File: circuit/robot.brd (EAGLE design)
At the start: 26 x 33 mm, 11 parts, among them M1 SERVO-FLIPPED, M2 SERVO-1, M3 SERVO-1, U1 ESP01

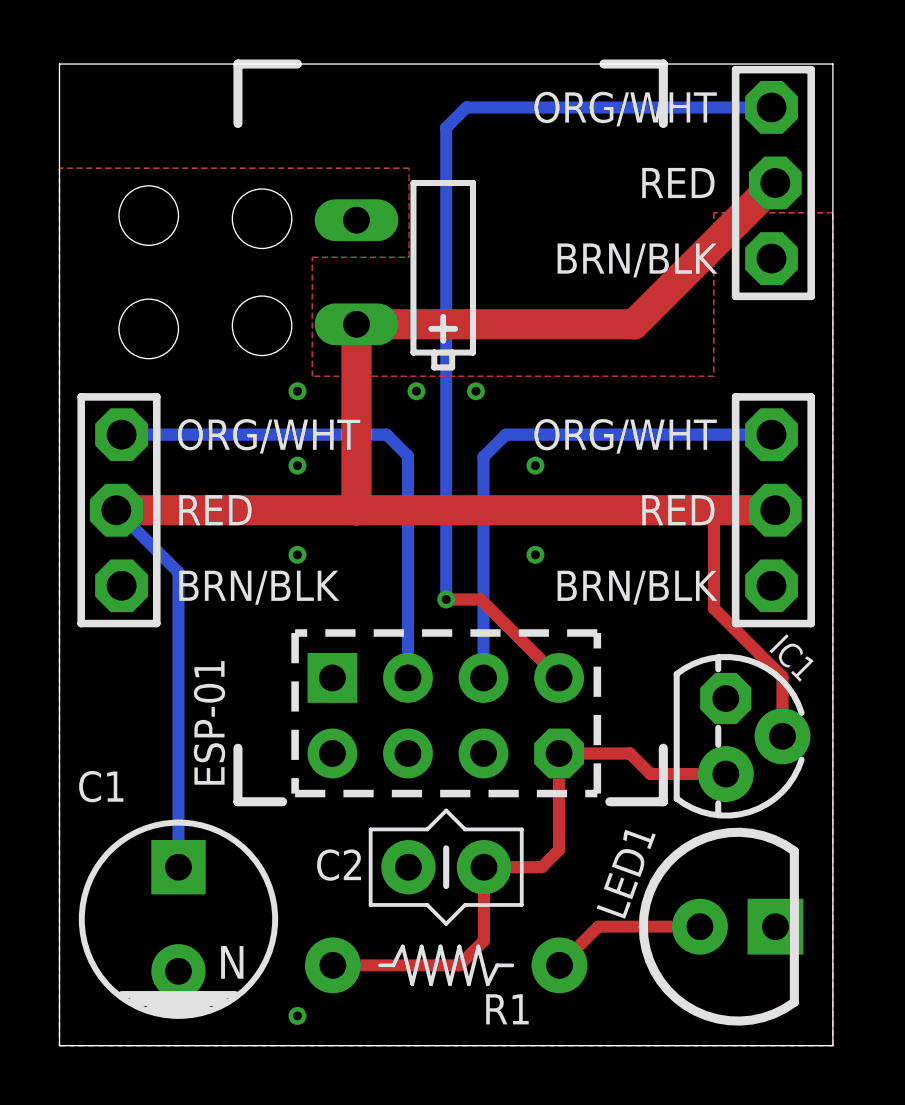
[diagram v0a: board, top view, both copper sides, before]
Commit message: update small PCB with version info
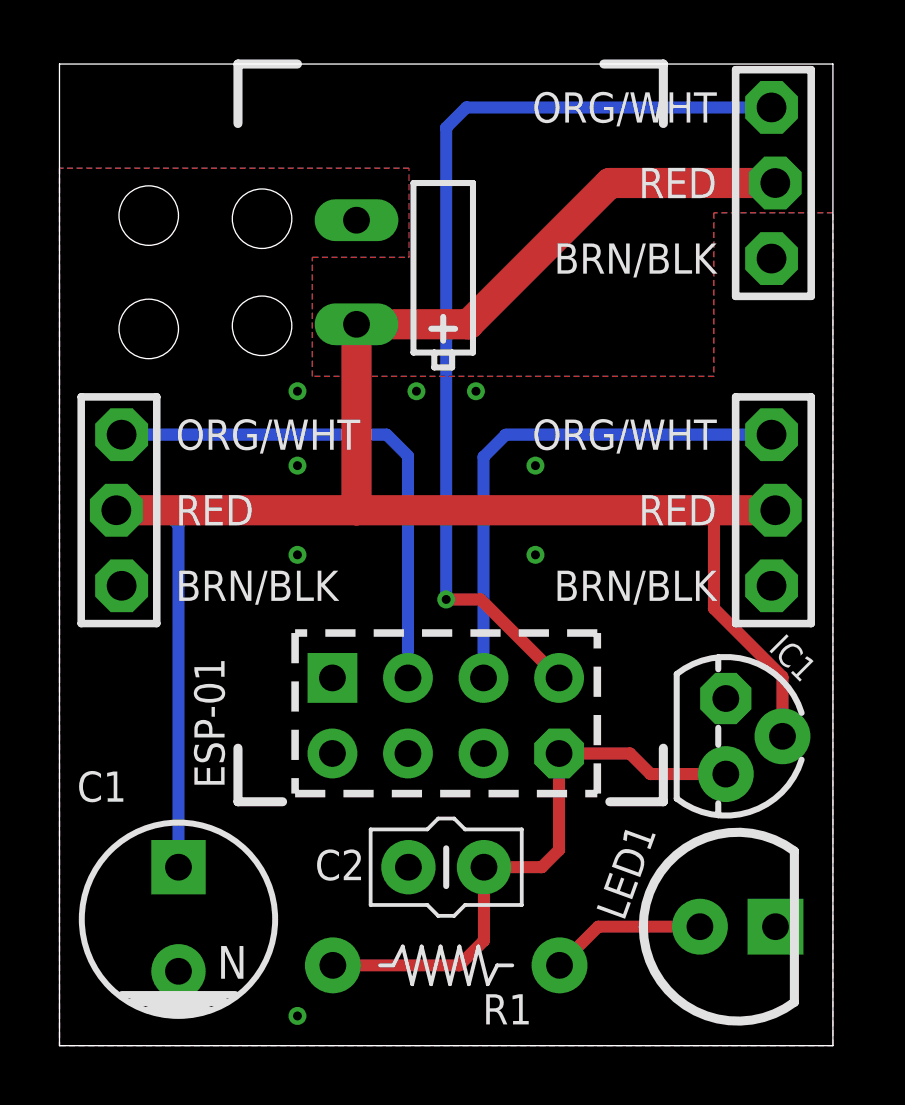
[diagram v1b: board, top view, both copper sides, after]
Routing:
- net +6V: track 65.9 -> 66.8 mm
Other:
- board text added: "SSF.NET/LIBRARY ROBOT-2019-REV1"
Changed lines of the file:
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@@
 <text x="5.3" y="2.25" size="1.1" layer="21" font="vector" ratio="12">N</text>
 <text x="5.55" y="8.65" size="1.016" layer="25" ratio="12" rot="R90">ESP-01</text>
+<text x="19.5" y="32.5" size="1.016" layer="22" rot="MR270">SSF.NET/LIBRARY
+ROBOT-2019-REV1</text>
 </plain>
 <attributes>
@@
 <wire x1="24.0635" y1="18" x2="22" y2="18" width="1.016" layer="1"/>
 <wire x1="22" y1="18" x2="9.985" y2="18" width="1.016" layer="1"/>
-<wire x1="24.0635" y1="29" x2="19.3135" y2="24.25" width="1.016" layer="1"/>
-<wire x1="19.3135" y1="24.25" x2="9.985" y2="24.25" width="1.016" layer="1"/>
 <wire x1="24.305" y1="10.4" x2="24.305" y2="12.395" width="0.4064" layer="1"/>
 <wire x1="24.305" y1="12.395" x2="22" y2="14.7" width="0.4064" layer="1"/>
 <wire x1="22" y1="14.7" x2="22" y2="18" width="0.4064" layer="1"/>
-<wire x1="4" y1="6" x2="4" y2="15.9111" width="0.4064" layer="16"/>
-<wire x1="4" y1="15.9111" x2="1.9111" y2="18" width="0.4064" layer="16"/>
+<wire x1="4" y1="6" x2="4" y2="17.5" width="0.4064" layer="16"/>
+<wire x1="4" y1="17.5" x2="3.5" y2="18" width="0.4064" layer="16"/>
+<wire x1="3.5" y1="18" x2="1.9111" y2="18" width="0.4064" layer="16"/>
+<wire x1="9.985" y1="24.25" x2="13.75" y2="24.25" width="1.016" layer="1"/>
+<wire x1="13.75" y1="24.25" x2="18.5" y2="29" width="1.016" layer="1"/>
+<wire x1="18.5" y1="29" x2="24.0635" y2="29" width="1.016" layer="1"/>
 </signal>
 <signal name="3.3V">
